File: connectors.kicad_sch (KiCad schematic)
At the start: 4 parts, among them J1 Conn_01x04_Pin, J2 Conn_01x04_Pin, J3 Conn_01x09_Pin, J4 Conn_02x03_Odd_Even

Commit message: completed symbol-footprint associations.
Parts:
- J1, J2: footprint (none) -> Connector_PinHeader_2.54mm:PinHeader_1x04_P2.54mm_Vertical
- J3: footprint (none) -> Connector_PinHeader_2.54mm:PinHeader_1x10_P2.54mm_Vertical
- J4: footprint (none) -> Connector_PinHeader_2.54mm:PinHeader_2x03_P2.54mm_Vertical
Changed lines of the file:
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@@
 			)
 		)
-		(property "Footprint" ""
+		(property "Footprint" "Connector_PinHeader_2.54mm:PinHeader_1x04_P2.54mm_Vertical"
 			(at 153.67 88.9 0)
 			(hide yes)
@@
 			)
 		)
-		(property "Footprint" ""
+		(property "Footprint" "Connector_PinHeader_2.54mm:PinHeader_1x10_P2.54mm_Vertical"
 			(at 200.66 95.25 0)
 			(hide yes)
@@
 			)
 		)
-		(property "Footprint" ""
+		(property "Footprint" "Connector_PinHeader_2.54mm:PinHeader_1x04_P2.54mm_Vertical"
 			(at 179.07 88.9 0)
 			(hide yes)
@@
 			)
 		)
-		(property "Footprint" ""
+		(property "Footprint" "Connector_PinHeader_2.54mm:PinHeader_2x03_P2.54mm_Vertical"
 			(at 153.67 116.84 0)
 			(hide yes)

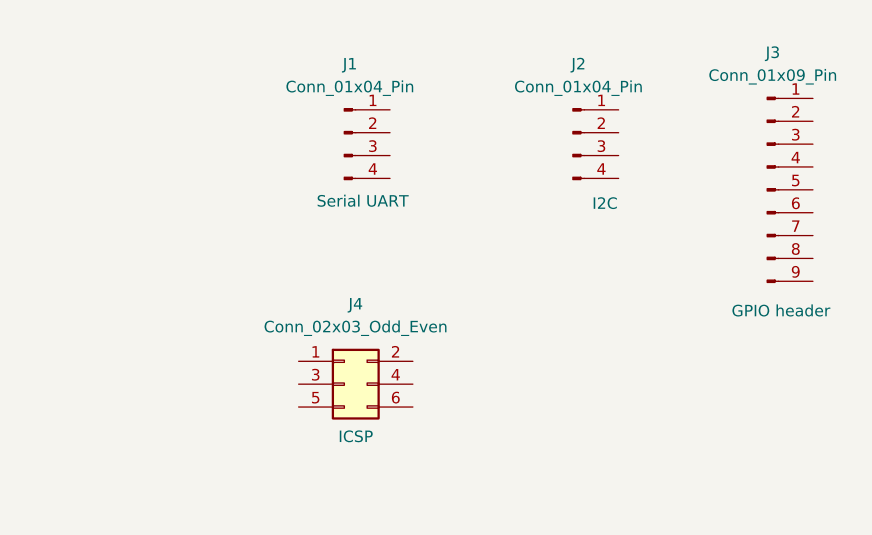
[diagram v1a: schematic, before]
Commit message: completed wiring in the second sheet.
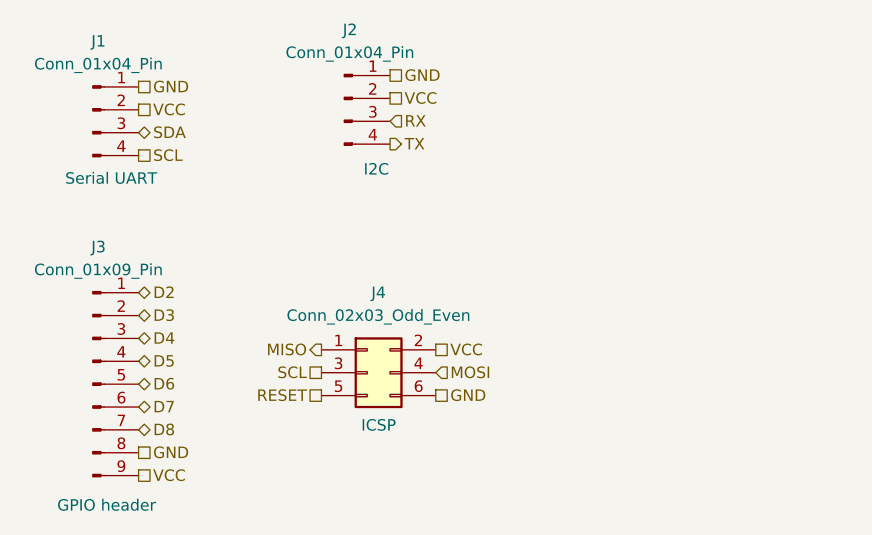
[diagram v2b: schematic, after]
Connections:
- net GND: now reaches J1.1 (Pin_1)
- net GND: now also J2.1 (Pin_1), J3.8 (Pin_8), J4.6 (Pin_6)
- net VCC: now reaches J1.2 (Pin_2)
- net VCC: now also J2.2 (Pin_2), J3.9 (Pin_9), J4.2 (Pin_2)
- net SDA: now reaches J1.3 (Pin_3)
- net SCL: now reaches J1.4 (Pin_4)
- net SCL: now also J4.3 (Pin_3)
- net D2: now reaches J3.1 (Pin_1)
- net D3: now reaches J3.2 (Pin_2)
- net D4: now reaches J3.3 (Pin_3)
- net D5: now reaches J3.4 (Pin_4)
- net D6: now reaches J3.5 (Pin_5)
- net D7: now reaches J3.6 (Pin_6)
- net D8: now reaches J3.7 (Pin_7)
- net RX: now reaches J2.3 (Pin_3)
- net TX: now reaches J2.4 (Pin_4)
- net MISO: now reaches J4.1 (Pin_1)
- net MOSI: now reaches J4.4 (Pin_4)
- net RESET: now reaches J4.5 (Pin_5)
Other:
- moved on the sheet: J1, J2, J3, J4

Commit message: Fixed defects in schematic
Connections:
- net SCL: no longer J4.3 (Pin_3)
- new net SCK: J4.3 (Pin_3)
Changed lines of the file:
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@@
 		)
 	)
-	(hierarchical_label "SCL"
+	(hierarchical_label "SCK"
 		(shape passive)
 		(at 151.13 115.57 180)
